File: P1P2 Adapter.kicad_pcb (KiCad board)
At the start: 2 copper layers, 31 parts, among them J1 Conn_01x07_Male, J2 Conn_01x01_Male, J3 Conn_01x01_Male, U1 MAX22088

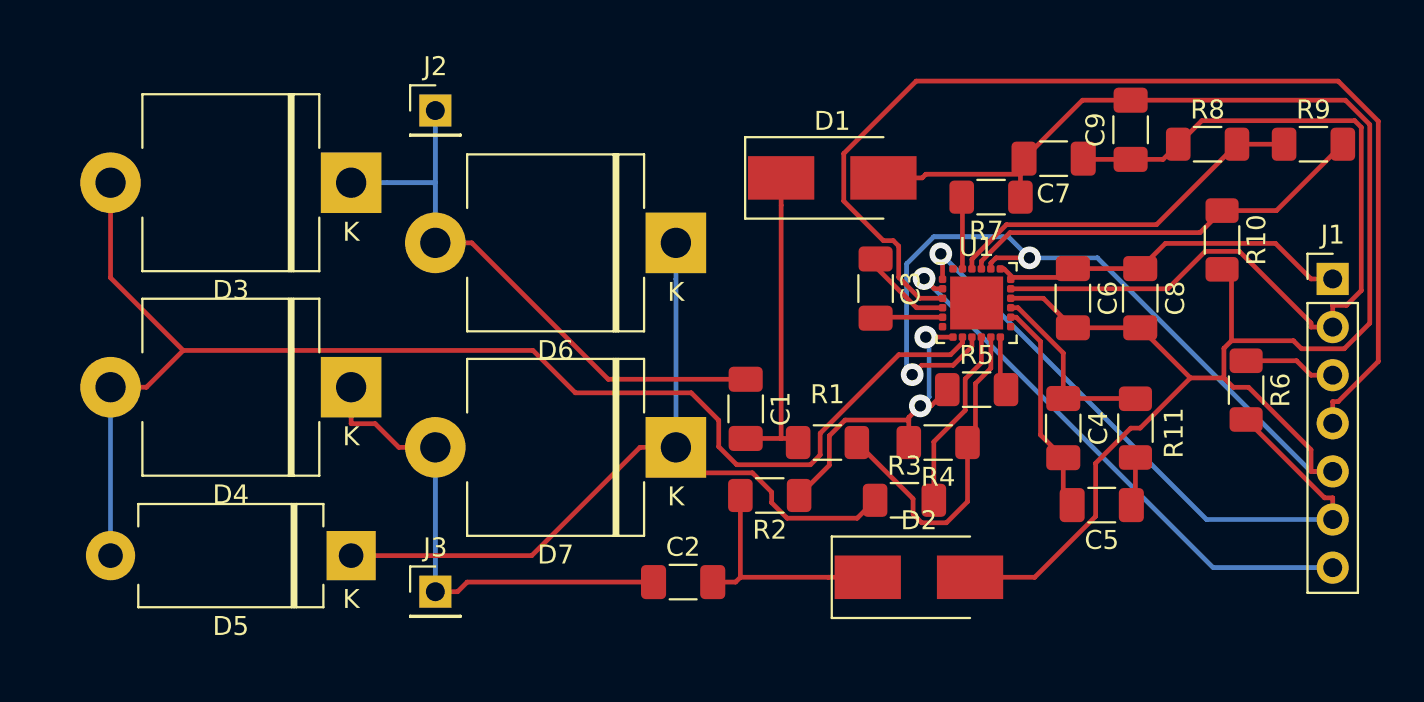
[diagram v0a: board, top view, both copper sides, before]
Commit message: Updated ground plane and PCB design
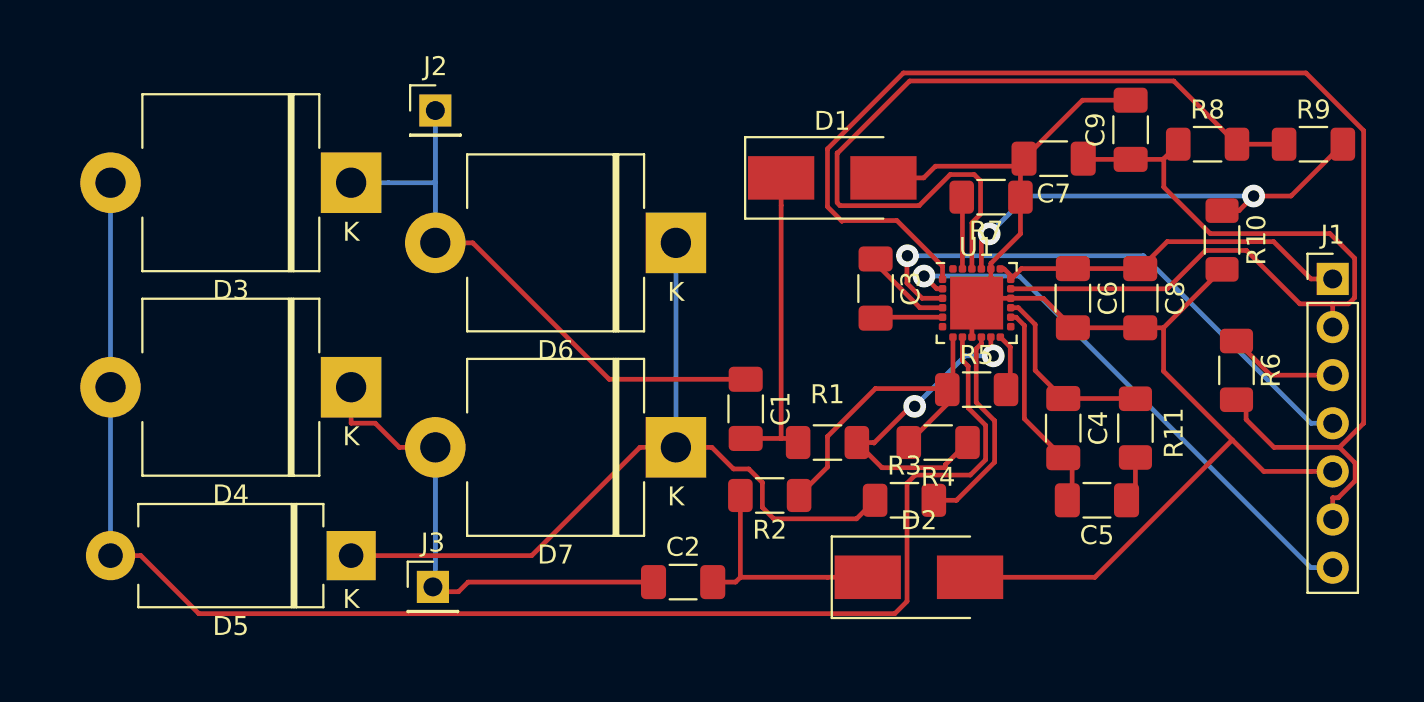
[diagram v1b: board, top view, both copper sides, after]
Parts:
- moved R6 1.16 mm to (139.4, 124.2)
- moved C5 0.36 mm to (132.1, 131.1)
- moved J3 0.28 mm to (97.0, 135.6)
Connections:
- U1 pad 25: (no net) -> GND
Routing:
- net GND: track 134.1 -> 70.2 mm, vias 2 -> 0
- net DOUT: track 35.3 -> 71.2 mm, vias 1 -> 0
- net RST: track 58.6 -> 29.8 mm, vias 0 -> 1
- net TVT: track 19.5 -> 42.4 mm
- net HN: track 72.1 -> 81.1 mm
- net +5V: track 46.9 -> 42.1 mm
- net TVL: track 22.0 -> 24.6 mm, vias 0 -> 2
- net HP: track 9.65 -> 11.2 mm
- net VLOGIC: track 4.89 -> 5.83 mm
- net AIO: track 17.7 -> 17.2 mm, vias 0 -> 2
- net BIO: track 17.7 -> 17.6 mm, vias 2 -> 0
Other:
- net class Default: clearance 0.25 -> 0.01
- rule trace_clearance: 0.25 -> 0.01

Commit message: Final touches, incl. design rule checks before having the board manufactured
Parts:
- moved R6 5.71 mm to (141.5, 129.5)
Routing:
- net GND: track 70.2 -> 75.7 mm
- net TVT: track 42.4 -> 47.2 mm
- net HN: track 81.1 -> 84.4 mm
- net HP: track 11.2 -> 13.3 mm
- net +5V: track 42.1 -> 43.7 mm
- net RST: track 29.8 -> 31.1 mm
- net DOUT: track 71.2 -> 72.4 mm
- net DIN: track 29.2 -> 30.1 mm
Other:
- board outline added: 71.1 x 33 mm
- net class Default: clearance 0.01 -> 0.16
- rule trace_clearance: 0.01 -> 0.16
- rule trace_min: 0.2 -> 0.25

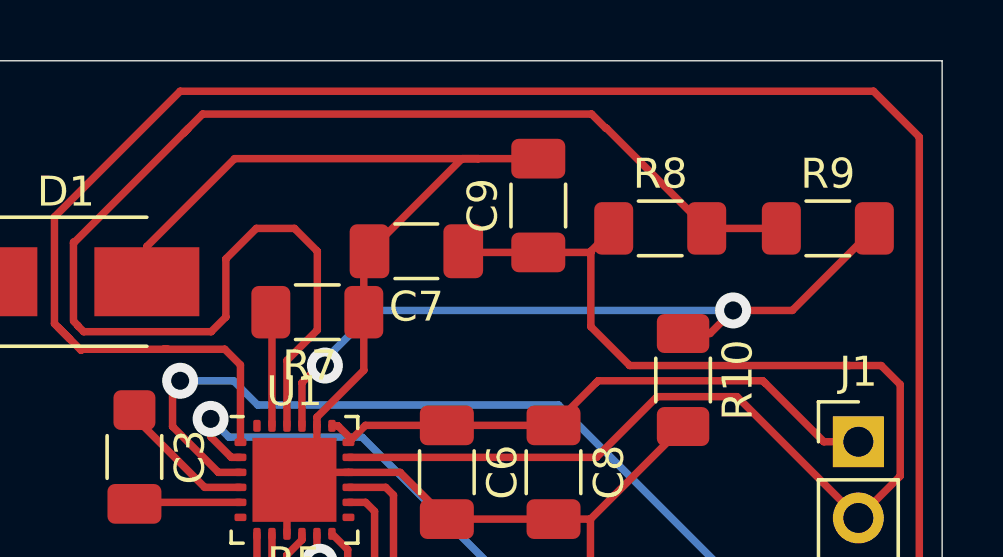
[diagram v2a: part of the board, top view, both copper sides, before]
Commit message: Fixed incorrect trim resistors and termination resistors. Credit goes to Arnold N, creator of P1P2Serial
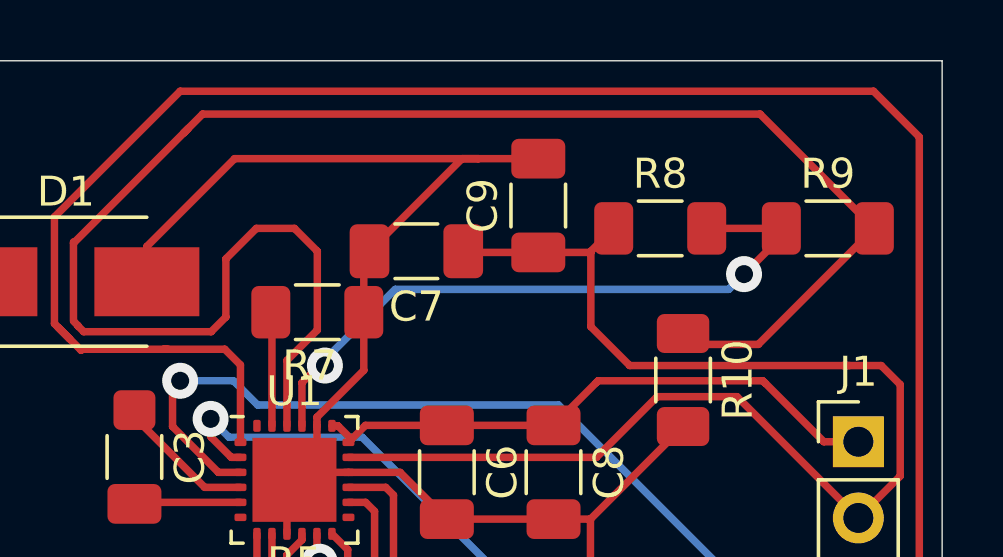
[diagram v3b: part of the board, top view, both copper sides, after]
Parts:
- R10: value 168k -> 20k
- R4: value 100 -> 1k
- R5: value 100 -> 82
- R8: value 1M -> 27k
- R9: value 220k -> 4.3k
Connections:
- R10 pad 1: TVL -> TVT
- R8 pad 2: TVT -> TVL
- R9 pad 1: TVT -> TVL
- R9 pad 2: TVL -> TVT
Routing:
- net TVT: track 47.2 -> 58.4 mm
- net TVL: track 24.6 -> 22.5 mm

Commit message: Made changes for 9600bps operation
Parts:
- C1, C2: value 1u -> 22u
- R4: value 1k -> 240
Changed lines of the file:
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@@
   (layers
     (0 F.Cu signal)
-    (31 B.Cu signal hide)
+    (31 B.Cu signal)
     (32 B.Adhes user hide)
     (33 F.Adhes user hide)
@@
       (effects (font (size 1 1) (thickness 0.15)))
     )
-    (fp_text value 1k (at 0 1.82) (layer F.Fab)
+    (fp_text value 240 (at 0 1.82) (layer F.Fab)
       (effects (font (size 1 1) (thickness 0.15)))
     )
@@
       (effects (font (size 0.8 0.8) (thickness 0.12)))
     )
-    (pad 2 smd roundrect (at 1.5625 0 90) (size 1.325 1.8) (layers F.Cu F.Paste F.Mask) (roundrect_rratio 0.1886777358490566)
+    (pad 2 smd roundrect (at 1.5625 0 90) (size 1.325 1.8) (layers F.Cu F.Paste F.Mask) (roundrect_rratio 0.1886769811320755)
       (net 10 GND))
-    (pad 1 smd roundrect (at -1.5625 0 90) (size 1.325 1.8) (layers F.Cu F.Paste F.Mask) (roundrect_rratio 0.1886777358490566)
+    (pad 1 smd roundrect (at -1.5625 0 90) (size 1.325 1.8) (layers F.Cu F.Paste F.Mask) (roundrect_rratio 0.1886769811320755)
       (net 12 +5V))
     (model ${KISYS3DMOD}/Capacitor_SMD.3dshapes/C_1206_3216Metric.wrl
@@
       (effects (font (size 0.8 0.8) (thickness 0.12)))
     )
-    (pad 2 smd roundrect (at 1.5625 0 270) (size 1.325 1.8) (layers F.Cu F.Paste F.Mask) (roundrect_rratio 0.1886777358490566)
+    (pad 2 smd roundrect (at 1.5625 0 270) (size 1.325 1.8) (layers F.Cu F.Paste F.Mask) (roundrect_rratio 0.1886769811320755)
       (net 10 GND))
-    (pad 1 smd roundrect (at -1.5625 0 270) (size 1.325 1.8) (layers F.Cu F.Paste F.Mask) (roundrect_rratio 0.1886777358490566)
+    (pad 1 smd roundrect (at -1.5625 0 270) (size 1.325 1.8) (layers F.Cu F.Paste F.Mask) (roundrect_rratio 0.1886769811320755)
       (net 11 +12V))
     (model ${KISYS3DMOD}/Capacitor_SMD.3dshapes/C_1206_3216Metric.wrl
@@
       (effects (font (size 0.8 0.8) (thickness 0.12)))
     )
-    (pad 2 smd roundrect (at 1.5625 0 180) (size 1.325 1.8) (layers F.Cu F.Paste F.Mask) (roundrect_rratio 0.1886777358490566)
+    (pad 2 smd roundrect (at 1.5625 0 180) (size 1.325 1.8) (layers F.Cu F.Paste F.Mask) (roundrect_rratio 0.1886769811320755)
       (net 10 GND))
-    (pad 1 smd roundrect (at -1.5625 0 180) (size 1.325 1.8) (layers F.Cu F.Paste F.Mask) (roundrect_rratio 0.1886777358490566)
+    (pad 1 smd roundrect (at -1.5625 0 180) (size 1.325 1.8) (layers F.Cu F.Paste F.Mask) (roundrect_rratio 0.1886769811320755)
       (net 12 +5V))
     (model ${KISYS3DMOD}/Capacitor_SMD.3dshapes/C_1206_3216Metric.wrl
@@
       (effects (font (size 0.8 0.8) (thickness 0.12)))
     )
-    (pad 2 smd roundrect (at 1.5625 0 270) (size 1.325 1.8) (layers F.Cu F.Paste F.Mask) (roundrect_rratio 0.1886777358490566)
+    (pad 2 smd roundrect (at 1.5625 0 270) (size 1.325 1.8) (layers F.Cu F.Paste F.Mask) (roundrect_rratio 0.1886769811320755)
       (net 10 GND))
-    (pad 1 smd roundrect (at -1.5625 0 270) (size 1.325 1.8) (layers F.Cu F.Paste F.Mask) (roundrect_rratio 0.1886777358490566)
+    (pad 1 smd roundrect (at -1.5625 0 270) (size 1.325 1.8) (layers F.Cu F.Paste F.Mask) (roundrect_rratio 0.1886769811320755)
       (net 11 +12V))
     (model ${KISYS3DMOD}/Capacitor_SMD.3dshapes/C_1206_3216Metric.wrl
@@
       (effects (font (size 0.8 0.8) (thickness 0.12)))
     )
-    (pad 2 smd roundrect (at 1.5625 0 180) (size 1.325 1.8) (layers F.Cu F.Paste F.Mask) (roundrect_rratio 0.1886777358490566)
+    (pad 2 smd roundrect (at 1.5625 0 180) (size 1.325 1.8) (layers F.Cu F.Paste F.Mask) (roundrect_rratio 0.1886769811320755)
       (net 7 HPA))
-    (pad 1 smd roundrect (at -1.5625 0 180) (size 1.325 1.8) (layers F.Cu F.Paste F.Mask) (roundrect_rratio 0.1886777358490566)
+    (pad 1 smd roundrect (at -1.5625 0 180) (size 1.325 1.8) (layers F.Cu F.Paste F.Mask) (roundrect_rratio 0.1886769811320755)
       (net 9 "Net-(C5-Pad1)"))
     (model ${KISYS3DMOD}/Capacitor_SMD.3dshapes/C_1206_3216Metric.wrl
@@
       (effects (font (size 0.8 0.8) (thickness 0.12)))
     )
-    (pad 2 smd roundrect (at 1.5625 0 270) (size 1.325 1.8) (layers F.Cu F.Paste F.Mask) (roundrect_rratio 0.1886777358490566)
+    (pad 2 smd roundrect (at 1.5625 0 270) (size 1.325 1.8) (layers F.Cu F.Paste F.Mask) (roundrect_rratio 0.1886769811320755)
       (net 7 HPA))
-    (pad 1 smd roundrect (at -1.5625 0 270) (size 1.325 1.8) (layers F.Cu F.Paste F.Mask) (roundrect_rratio 0.1886777358490566)
+    (pad 1 smd roundrect (at -1.5625 0 270) (size 1.325 1.8) (layers F.Cu F.Paste F.Mask) (roundrect_rratio 0.1886769811320755)
       (net 8 CAPP))
     (model ${KISYS3DMOD}/Capacitor_SMD.3dshapes/C_1206_3216Metric.wrl
@@
       (effects (font (size 0.8 0.8) (thickness 0.12)))
     )
-    (pad 2 smd roundrect (at 1.5625 0 270) (size 1.325 1.8) (layers F.Cu F.Paste F.Mask) (roundrect_rratio 0.1886777358490566)
+    (pad 2 smd roundrect (at 1.5625 0 270) (size 1.325 1.8) (layers F.Cu F.Paste F.Mask) (roundrect_rratio 0.1886769811320755)
       (net 5 "Net-(C3-Pad2)"))
     (pad 1 smd roundrect (at -1.5625 0 270) (size 1.325 1.4) (layers F.Cu F.Paste F.Mask) (roundrect_rratio 0.189)
@@
       (effects (font (size 1 1) (thickness 0.15)))
     )
-    (fp_text value 1u (at 0 1.85) (layer F.Fab)
+    (fp_text value 22u (at 0 1.85) (layer F.Fab)
       (effects (font (size 1 1) (thickness 0.15)))
     )
@@
       (effects (font (size 0.8 0.8) (thickness 0.12)))
     )
-    (pad 2 smd roundrect (at 1.5625 0) (size 1.325 1.8) (layers F.Cu F.Paste F.Mask) (roundrect_rratio 0.1886777358490566)
+    (pad 2 smd roundrect (at 1.5625 0) (size 1.325 1.8) (layers F.Cu F.Paste F.Mask) (roundrect_rratio 0.1886769811320755)
       (net 3 "Net-(C2-Pad2)"))
-    (pad 1 smd roundrect (at -1.5625 0) (size 1.325 1.8) (layers F.Cu F.Paste F.Mask) (roundrect_rratio 0.1886777358490566)
+    (pad 1 smd roundrect (at -1.5625 0) (size 1.325 1.8) (layers F.Cu F.Paste F.Mask) (roundrect_rratio 0.1886769811320755)
       (net 4 P2))
     (model ${KISYS3DMOD}/Capacitor_SMD.3dshapes/C_1206_3216Metric.wrl
@@
       (effects (font (size 1 1) (thickness 0.15)))
     )
-    (fp_text value 1u (at 0 1.85 90) (layer F.Fab)
+    (fp_text value 22u (at 0 1.85 90) (layer F.Fab)
       (effects (font (size 1 1) (thickness 0.15)))
     )
@@
       (effects (font (size 0.8 0.8) (thickness 0.12)))
     )
-    (pad 2 smd roundrect (at 1.5625 0 270) (size 1.325 1.8) (layers F.Cu F.Paste F.Mask) (roundrect_rratio 0.1886777358490566)
+    (pad 2 smd roundrect (at 1.5625 0 270) (size 1.325 1.8) (layers F.Cu F.Paste F.Mask) (roundrect_rratio 0.1886769811320755)
       (net 1 "Net-(C1-Pad2)"))
-    (pad 1 smd roundrect (at -1.5625 0 270) (size 1.325 1.8) (layers F.Cu F.Paste F.Mask) (roundrect_rratio 0.1886777358490566)
+    (pad 1 smd roundrect (at -1.5625 0 270) (size 1.325 1.8) (layers F.Cu F.Paste F.Mask) (roundrect_rratio 0.1886769811320755)
       (net 2 P1))
     (model ${KISYS3DMOD}/Capacitor_SMD.3dshapes/C_1206_3216Metric.wrl
@@
   (segment (start 124.98 115.1) (end 124.98 118.85) (width 0.25) (layer F.Cu) (net 23))
   (segment (start 118.364 112.7185) (end 118.364 115.316) (width 0.25) (layer F.Cu) (net 24))
-  (segment (start 141.96 112.268) (end 139.472 112.268) (width 0.25) (layer F.Cu) (net 25))
   (segment (start 122.0399 109.0859) (end 122.1956 108.9302) (width 0.25) (layer F.Cu) (net 24))
   (segment (start 118.364 112.7618) (end 122.0399 109.0859) (width 0.25) (layer F.Cu) (net 24))
@@
   (segment (start 139.046867 116.134867) (end 138.684 115.772) (width 0.25) (layer F.Cu) (net 24))
   (segment (start 141.193133 116.134867) (end 139.046867 116.134867) (width 0.25) (layer F.Cu) (net 24))
+  (segment (start 141.96 112.268) (end 139.472 112.268) (width 0.25) (layer F.Cu) (net 25))
   (segment (start 125.98 118.85) (end 125.98 117.4104) (width 0.25) (layer F.Cu) (net 25))
   (segment (start 125.98 117.4104) (end 126.3929 116.9975) (width 0.25) (layer F.Cu) (net 25))
